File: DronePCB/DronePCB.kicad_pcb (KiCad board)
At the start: 4 copper layers, 161 parts, among them J1 VBUS, J2 PD_SCL, J3 PD_SDA, J4 SysPower, J5 UART, J6 5V, J7 3V3, J8 Battery, J9 USB_C_Receptacle_PowerOnly_6P, M1 Motor_DC, M2 Motor_DC, Q1 AO3400A, Q10 AO3401A, Q11 AO3401A, Q2 AO3400A, Q3 SiS454DN, Q4 SiS454DN, Q5 AO3400A, Q6 AO3400A, Q7 AO3400A, Q8 AO3401A, Q9 AO3401A, U1 RASPBERRY_PI_ZERO_2_W, U10 DRV8231DDAR, U2 CC1101RGPR, U3 BQ24725A, U4 CYPD3177-24LQXQT, U5 DMP3098LSD-13, U6 DMP3098LSD-13, U7 LMR33630BDDA, U8 TSOP45xx, U9 DRV8231DDAR, Y1 Crystal_GND24

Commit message: finished H bridge pcb design
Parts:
- removed R48: 100, Resistor_SMD:R_0603_1608Metric
- removed R49: 10k, Resistor_SMD:R_0603_1608Metric
- moved C46 80.6 mm to (181.5, 150.8)
- moved C48 69.5 mm to (181.5, 143.0)
- moved M1 51.2 mm to (189.1, 134.8), turned to 90 degrees
- moved U9 46.1 mm to (178.8, 134.5)
- moved Q8 44.0 mm to (172.5, 136.7), turned to 90 degrees
- moved C50 39.2 mm to (183.5, 137.5), turned to -90 degrees
- moved C52 38.7 mm to (185.2, 137.5), turned to -90 degrees
- moved Q9 37.6 mm to (172.5, 132.2), turned to -90 degrees
- moved R39 24.2 mm to (176.9, 130.5)
- moved R44 20.5 mm to (172.5, 139.8), turned to 180 degrees
- moved R36 19.5 mm to (166.0, 133.2)
- moved R41 18.5 mm to (172.5, 129.0), turned to 180 degrees
- moved R35 18.3 mm to (166.0, 135.8)
- moved R42 17.1 mm to (166.0, 137.8)
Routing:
- net Net-(Q8-G): track 0.00 -> 16.7 mm, vias 0 -> 2
- net +3V3: track 31.5 -> 47.2 mm, vias 4 -> 6
- net Net-(Q8-D): track 0.00 -> 9.65 mm
- net Net-(Q9-D): track 0.00 -> 9.64 mm
- net Net-(Q10-G): track 6.34 -> 13.5 mm, vias 0 -> 2
- net Net-(U9-IPROPI): track 0.00 -> 2.14 mm
- net GND: vias 37 -> 56
- added copper zone on F.Cu, net Net-(M1-+)
- added copper zone on F.Cu, net Net-(M1--)

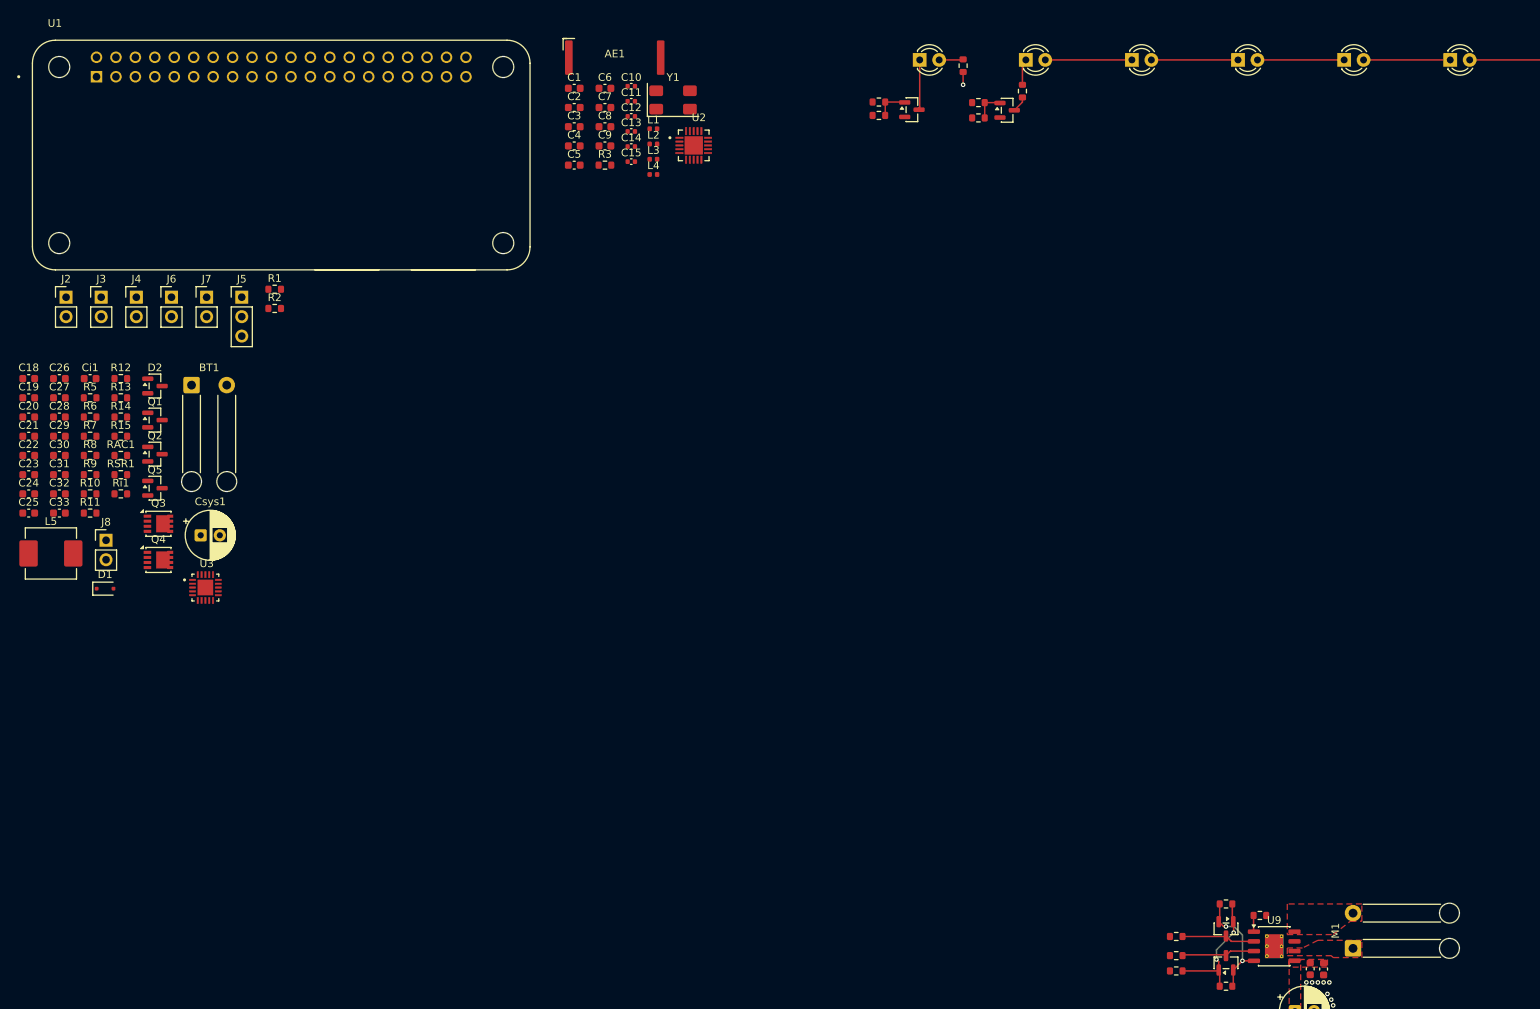
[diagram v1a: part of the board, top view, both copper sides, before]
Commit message: Finished CC1101 Radio Circuit
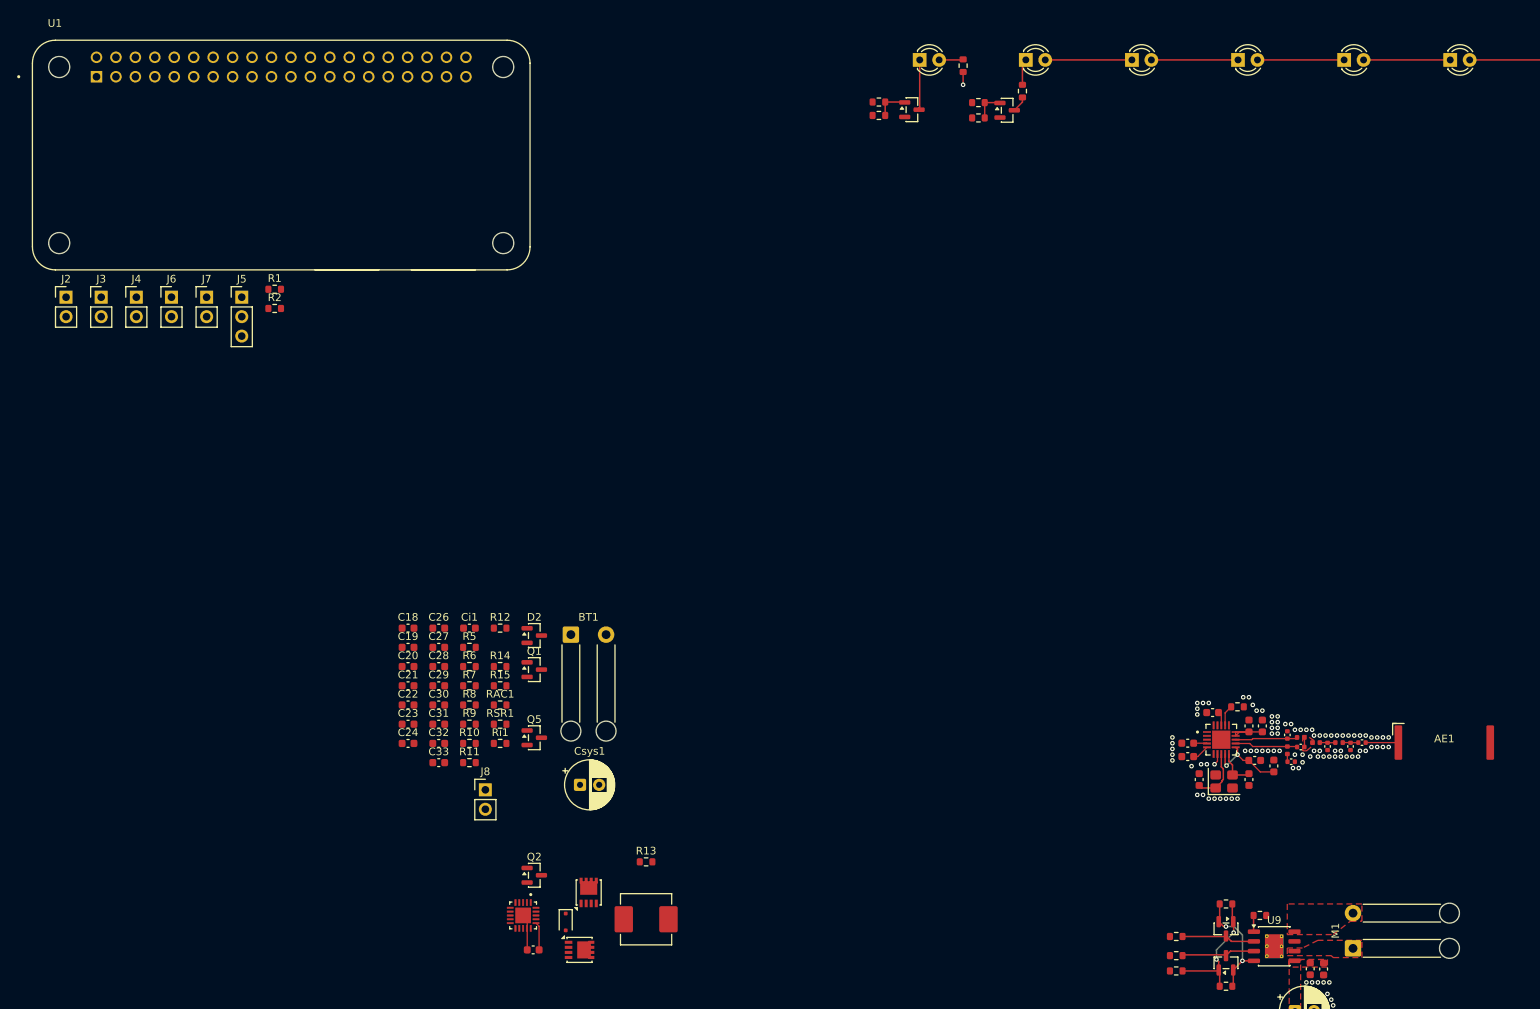
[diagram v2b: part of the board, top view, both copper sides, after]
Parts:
- Y1: value Crystal_GND24 -> NX3225GA; footprint Crystal:Crystal_SMD_0603-4Pin_6.0x3.5mm -> Crystal:Crystal_SMD_3225-4Pin_3.2x2.5mm
- moved AE1 140.5 mm to (201.0, 107.9)
- moved C2 125.5 mm to (178.8, 111.0), turned to 90 degrees
- moved C1 124.9 mm to (176.2, 110.2)
- moved C10 123.4 mm to (181.0, 110.4)
- moved C14 122.3 mm to (188.8, 108.4), turned to -90 degrees
- moved C15 121.9 mm to (190.3, 107.9)
- moved C13 121.3 mm to (185.8, 108.4), turned to -90 degrees
- moved C12 120.1 mm to (182.3, 108.5), turned to 180 degrees
- moved C11 119.1 mm to (180.5, 106.9), turned to -90 degrees
- moved C9 118.0 mm to (175.5, 112.8), turned to -90 degrees
- moved C3 117.9 mm to (175.5, 105.8), turned to 90 degrees
- moved C4 117.6 mm to (177.2, 105.8), turned to 90 degrees
- moved L4 116.3 mm to (187.3, 107.9), turned to 180 degrees
- moved L1 116.0 mm to (180.5, 108.9), turned to -90 degrees
- moved C6 115.8 mm to (167.5, 109.8), turned to 180 degrees
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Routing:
- net +3V3: track 47.2 -> 67.5 mm, vias 6 -> 8
- net Net-(U2-RF_N): track 0.00 -> 8.37 mm
- net Net-(U2-RF_P): track 0.00 -> 8.20 mm
- net XTAL_Q1: track 0.00 -> 7.25 mm
- net XTAL_Q2: track 0.00 -> 5.16 mm
- net GND: track 6.12 -> 10.9 mm, vias 56 -> 141
- net Net-(AE1-A): track 0.00 -> 4.27 mm
- net Net-(D1-A): track 0.00 -> 3.67 mm
- net Net-(U2-RBIAS): track 0.00 -> 2.75 mm
- net Net-(C14-Pad1): track 0.00 -> 2.05 mm
- net Net-(C13-Pad1): track 0.00 -> 2.05 mm
- net Net-(U2-DGUARD): track 0.00 -> 1.82 mm
- net /CC1101Radio/CSN: track 0.00 -> 1.50 mm, vias 0 -> 1
- net Net-(C10-Pad1): track 0.00 -> 1.02 mm
- net Net-(C12-Pad1): track 0.00 -> 1.00 mm
- added copper zone on F.Cu, net Net-(C12-Pad1)

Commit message: All circuits complete
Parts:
- removed BT1: Battery, Connector_Wire:SolderWire-0.5sqmm_1x02_P4.6mm_D0.9mm_OD2.1mm_Relief
- removed Ci1: 2.2 uF, Capacitor_SMD:C_0603_1608Metric
- removed Csys1: 220 uF, Capacitor_THT:CP_Radial_D6.3mm_P2.50mm
- removed the J8 at (75.8, 114.1)
- removed the Q4 at (88.1, 135.0)
- removed the Q5 at (82.1, 107.3)
- removed R10: 316 k ohms, Resistor_SMD:R_0603_1608Metric
- removed R8: 4.02 k ohms, Resistor_SMD:R_0603_1608Metric
- removed Ri1: 2 ohms, Resistor_SMD:R_0603_1608Metric
- added J9: Batt, Connector_Wire:SolderWire-0.25sqmm_1x02_P4.2mm_D0.65mm_OD1.7mm_Relief, F.Cu at (144.6, 121.1)
- added MOSFET1: SIS412DN-T1-GE3, Package_SO:Vishay_PowerPAK_1212-8_Single, F.Cu at (120.0, 109.1)
- added MOSFET2: SIS412DN-T1-GE3, Package_SO:Vishay_PowerPAK_1212-8_Single, F.Cu at (120.0, 104.3)
- added R16: 10 ohms, Resistor_SMD:R_0603_1608Metric, F.Cu at (127.5, 116.3)
- added R17: 7.5 ohms, Resistor_SMD:R_0603_1608Metric, F.Cu at (131.3, 119.8)
- C18: footprint Capacitor_SMD:C_0603_1608Metric -> Capacitor_SMD:C_1210_3225Metric
- C29, C30, C32, C33, C41: footprint Capacitor_SMD:C_0603_1608Metric -> Capacitor_SMD:C_1206_3216Metric
- Q1, Q2: footprint Package_TO_SOT_SMD:SOT-23 -> Package_SO:SO-8_3.9x4.9mm_P1.27mm
- Q3: value SiS454DN -> AO3400A; footprint Package_SO:Vishay_PowerPAK_1212-8_Single -> Package_SO:SO-8_3.9x4.9mm_P1.27mm
- R11: value 10 k ohms -> 100 k ohms
- R12: value 10 ohms -> 316 k ohms
- R13: value 4.02 k ohms -> 10 k ohms
- R15: value 7.5 ohms -> 4.02 k ohms
- R9: value 100 k ohms -> 4.02 k ohms
- moved C53 163.4 mm to (123.1, 33.9), turned to 0 degrees
- moved M2 158.7 mm to (115.5, 49.6), turned to -90 degrees
- moved C51 154.6 mm to (123.0, 41.1), turned to 0 degrees
- moved C55 154.6 mm to (119.3, 46.9), turned to 90 degrees
- moved C57 151.6 mm to (121.0, 46.9), turned to 90 degrees
- moved U10 140.5 mm to (125.8, 49.8), turned to 180 degrees
- moved R39 135.6 mm to (132.3, 44.6), turned to 180 degrees
- moved R47 133.5 mm to (127.5, 53.6), turned to 180 degrees
- moved Q8 132.0 mm to (132.3, 47.6), turned to -90 degrees
- moved R36 128.9 mm to (135.8, 45.6), turned to 180 degrees
- moved Q9 127.3 mm to (132.3, 51.8), turned to 90 degrees
- moved R44 125.2 mm to (135.8, 48.6), turned to 180 degrees
- moved R40 124.3 mm to (132.3, 54.6), turned to 180 degrees
- moved R45 123.1 mm to (135.8, 50.4), turned to 180 degrees
- moved M1 118.2 mm to (265.5, 44.6)
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- renumbered C57 to C43, C43 to C44, C44 to C45, C54 to C46, C55 to C47, C56 to C48, C45 to C49, C46 to C50, C47 to C51, C48 to C52, C49 to C53, C50 to C54, C51 to C55, C52 to C56, C53 to C57, J9 to J8, Q6 to Q4, Q7 to Q5, Q8 to Q6, Q9 to Q7, Q10 to Q8, Q11 to Q9, R16 to R18, R18 to R19, R19 to R20, R20 to R21, R21 to R22, R22 to R23, R23 to R24, R24 to R25, R25 to R26, R26 to R27, R27 to R28, R28 to R29, R29 to R30, R30 to R31, R31 to R32, R32 to R33, R33 to R34, R34 to R35, R45 to R36, R42 to R37, R44 to R38, R50 to R39, R46 to R40, R35 to R42, R36 to R43, R37 to R44, R38 to R45, R39 to R46, R40 to R47
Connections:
- C18 pad 2: Net-(Q1-G) -> Net-(C18-Pad2)
- C19 pad 1: Net-(Q1-S) -> Net-(C19-Pad1)
- C19 pad 2: Net-(Q1-G) -> Net-(C18-Pad2)
- C20 pad 1: Net-(Q2-S) -> Net-(U3-ACP)
- C21 pad 2: Net-(Q2-S) -> Net-(U3-ACP)
- C24 pad 2: Net-(Q4-D) -> Net-(U3-PHASE)
- C27 pad 2: Net-(Q5-S) -> Net-(J9-Pin_1)
- C28 pad 1: Net-(Q5-S) -> Net-(J9-Pin_1)
- C31 pad 1: Net-(Q5-G) (its old number) -> Net-(C31-Pad1)
- C31 pad 2: Net-(Q5-S) -> Net-(J9-Pin_1)
- C32 pad 1: Net-(J8-Pin_2) -> Net-(J9-Pin_1)
- C33 pad 1: Net-(J8-Pin_2) -> Net-(J9-Pin_1)
- L5 pad 1: Net-(Q4-D) -> Net-(U3-PHASE)
- Q1 pad 1: Net-(Q1-G) -> Net-(C19-Pad1)
- Q1 pad 2: Net-(Q1-S) -> Net-(C19-Pad1)
- Q1 pad 3: /Battery Charger/VBUS -> Net-(C19-Pad1)
- Q2 pad 1: Net-(Q1-G) -> Net-(C19-Pad1)
- Q2 pad 2: Net-(Q2-S) -> Net-(C19-Pad1)
- Q2 pad 3: Net-(Q1-S) -> Net-(C19-Pad1)
- Q3 pad 1: Net-(Q4-D) -> Net-(J9-Pin_1)
- Q3 pad 2: Net-(Q4-D) -> Net-(J9-Pin_1)
- Q3 pad 3: Net-(Q4-D) -> Net-(J9-Pin_1)
- Q3 pad 4: Net-(Q3-G) -> Net-(C31-Pad1)
- R11 pad 1: +3V3 -> Net-(U3-ILIM)
- R11 pad 2: ACOK -> GND
- R12 pad 1: Net-(D2-Pad3) -> +3V3
- R12 pad 2: Net-(U3-VCC) -> Net-(U3-ILIM)
- R13 pad 1: Net-(U3-BATDRV) -> +3V3
- R13 pad 2: Net-(Q5-G) (its old number) -> ACOK
- R14 pad 1: Net-(U3-SRP) -> Net-(D2-Pad3)
- R14 pad 2: Net-(C27-Pad1) -> Net-(U3-VCC)
- R15 pad 1: Net-(Q5-S) -> Net-(U3-BATDRV)
- R15 pad 2: Net-(U3-SRN) -> Net-(C31-Pad1)
- R7 pad 1: Net-(Q1-G) -> Net-(C18-Pad2)
- R9 pad 1: Net-(U3-ILIM) -> Net-(C19-Pad1)
- R9 pad 2: GND -> Net-(U3-CMSRC)
- RAC1 pad 1: Net-(Q2-S) -> Net-(U3-ACP)
- RSR1 pad 2: Net-(J8-Pin_2) -> Net-(J9-Pin_1)
- U3 pad 18: Net-(Q3-G) -> Net-(MOSFET2-G)
- U3 pad 19: Net-(Q4-D) -> Net-(U3-PHASE)
- U3 pad 2: Net-(Q2-S) -> Net-(U3-ACP)
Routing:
- net /Battery Charger/VBUS: track 0.00 -> 30.1 mm, vias 0 -> 2
- net Net-(U3-VCC): track 0.00 -> 18.0 mm, vias 0 -> 2
- net Net-(C31-Pad1): track 0.00 -> 17.9 mm, vias 0 -> 2
- net Net-(D1-K): track 0.00 -> 15.2 mm
- net Net-(C18-Pad2): track 0.00 -> 9.52 mm, vias 0 -> 2
- net VDD: track 10.5 -> 1.68 mm
- net Net-(U3-SRN): track 0.00 -> 8.69 mm
- net ACOK: track 0.00 -> 8.13 mm, vias 0 -> 2
- net Net-(U3-CMSRC): track 0.00 -> 7.99 mm, vias 0 -> 2
- net Net-(U3-PHASE): track 0.00 -> 7.64 mm
- net GND: track 10.9 -> 18.1 mm, vias 141 -> 158
- net Net-(MOSFET1-G): track 0.00 -> 6.58 mm, vias 0 -> 2
- net Net-(U3-ACDET): track 0.00 -> 6.22 mm
- net Net-(U3-ACDRV): track 0.00 -> 5.27 mm
- net /Battery Charger/SystemPower: track 0.00 -> 4.47 mm, vias 0 -> 36
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- added copper zone on F.Cu, net /Battery Charger/SystemPower
- added copper zone on In2.Cu, net /Battery Charger/SystemPower
- added copper zone on F.Cu, net /Battery Charger/VBUS
- added copper zone on F.Cu, net Net-(C18-Pad2)
- added copper zone on F.Cu, net Net-(C19-Pad1)
- added copper zone on F.Cu, net Net-(C27-Pad1)
- added copper zone on F.Cu, net Net-(J9-Pin_1)
- added copper zone on F.Cu, net Net-(U3-ACP)
- added copper zone on F.Cu, net Net-(U3-PHASE)
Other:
- board text added: "VIN"

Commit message: Rough board placement complete
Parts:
- D10, D3, D4, D5, D6, D7, D8, D9: footprint LED_THT:LED_D3.0mm_IRBlack -> LED_THT:LED_D5.0mm_IRGrey; moved to B.Cu
- J5, U8: moved to B.Cu
- moved J2 185.3 mm to (200.6, 95.5), turned to 180 degrees
- moved J3 183.9 mm to (204.3, 93.0)
- moved J4 117.0 mm to (135.4, 101.0), turned to 90 degrees
- moved J5 113.4 mm to (156.5, 64.1), turned to -90 degrees
- moved J6 112.6 mm to (144.4, 75.3), turned to 90 degrees
- moved U1 108.1 mm to (173.0, 81.2)
- moved J7 98.8 mm to (135.5, 72.2), turned to 90 degrees
- moved R1 90.6 mm to (136.4, 69.5)
- moved R2 89.7 mm to (136.4, 67.9)
- moved C41 80.8 mm to (147.7, 82.0)
- moved C43 80.8 mm to (162.9, 82.4)
- moved C44 80.8 mm to (162.2, 80.1)
- moved C45 80.8 mm to (148.5, 78.8)
- moved C47 80.8 mm to (151.9, 78.8)
- moved C48 80.8 mm to (150.2, 78.8)
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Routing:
- net Net-(J7-Pin_2): track 0.00 -> 34.3 mm
- net +3V3: track 70.4 -> 91.1 mm
- net +5V: track 0.00 -> 19.0 mm
- net /Battery Charger/SCL: track 1.88 -> 20.1 mm
- net /Battery Charger/SDA: track 2.09 -> 19.8 mm, vias 1 -> 2
- net /USB_PD/SCL: track 1.01 -> 13.2 mm, vias 1 -> 2
- net /USB_PD/SDA: track 1.65 -> 9.57 mm, vias 1 -> 2
- net TX: track 0.00 -> 4.39 mm
- net RX: track 0.00 -> 4.39 mm
- net Net-(D4-K): track 3.43 -> 4.23 mm
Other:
- board outline added: 158 x 68 mm

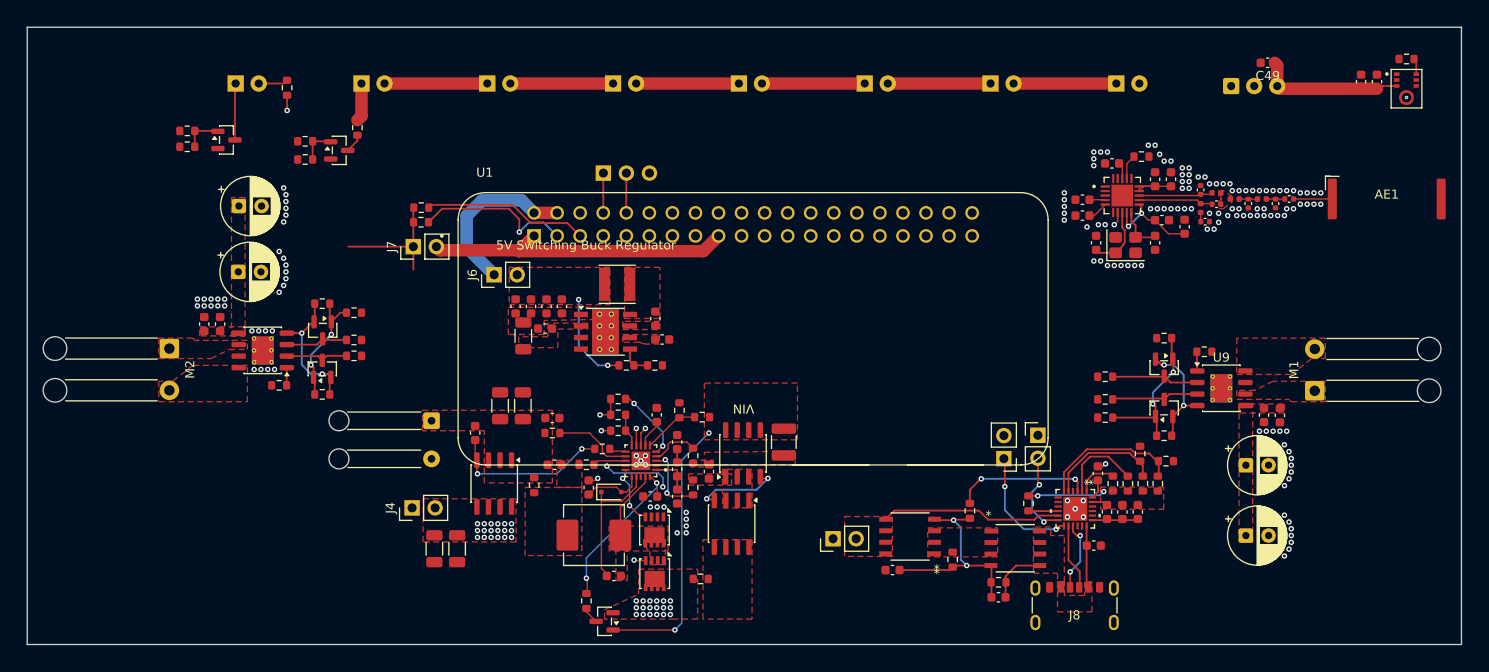
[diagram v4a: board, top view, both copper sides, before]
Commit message: Changed Resistor on IR Blaster | Finished Running DRC on PCB
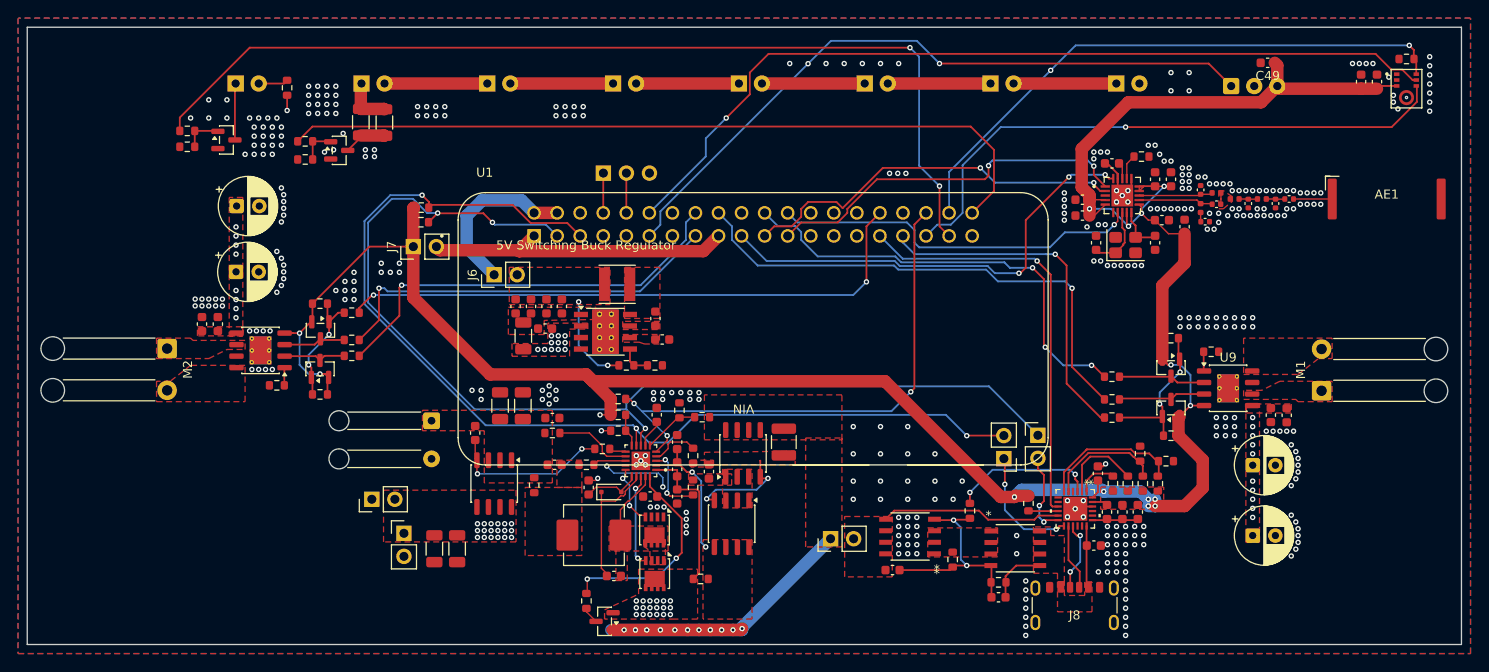
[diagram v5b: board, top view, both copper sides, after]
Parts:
- added J10: SysPower, Connector_PinHeader_2.54mm:PinHeader_1x02_P2.54mm_Vertical, F.Cu at (134.5, 103.8)
- added R48: 68, Resistor_SMD:R_1206_3216Metric, F.Cu at (132.3, 58.5)
- R33: value 35 -> 68; footprint Resistor_SMD:R_0603_1608Metric -> Resistor_SMD:R_1206_3216Metric
- moved J4 4.54 mm to (131.0, 100.0)
- moved C50 0.75 mm to (228.0, 104.0)
- moved C52 0.75 mm to (228.0, 96.2)
- moved C54 0.75 mm to (230.0, 90.7)
- moved C56 0.75 mm to (231.8, 90.8)
- moved M1 0.75 mm to (235.6, 88.0)
- moved Q6 0.75 mm to (219.0, 89.9)
- moved Q7 0.75 mm to (219.0, 85.5)
- moved R37 0.75 mm to (212.5, 91.0)
- moved R38 0.75 mm to (219.0, 93.0)
- moved R41 0.75 mm to (219.0, 82.2)
- moved R42 0.75 mm to (212.5, 89.0)
- moved R43 0.75 mm to (212.5, 86.5)
- moved R46 0.75 mm to (223.4, 83.8)
- moved U9 0.75 mm to (225.3, 87.8)
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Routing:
- net +3V3: track 91.1 -> 260.0 mm, vias 9 -> 15
- net IR_Out: track 0.00 -> 107.6 mm, vias 0 -> 2
- net /Battery Charger/SDA: track 19.8 -> 121.2 mm, vias 2 -> 3
- net /Battery Charger/SCL: track 20.1 -> 117.5 mm, vias 1 -> 3
- net /I2S Microphone/SCK: track 0.00 -> 95.5 mm, vias 0 -> 1
- net IR_Blaster: track 0.00 -> 86.4 mm
- net IR_In: track 0.00 -> 75.9 mm, vias 0 -> 2
- net /H-Bridge/EN_R: track 0.00 -> 65.8 mm, vias 0 -> 2
- net /I2S Microphone/WS: track 0.00 -> 65.0 mm, vias 0 -> 1
- net /I2S Microphone/SD: track 1.77 -> 64.5 mm, vias 0 -> 2
- net IN1_L: track 0.00 -> 57.0 mm, vias 0 -> 1
- net ACOK: track 8.13 -> 59.5 mm, vias 2 -> 3
- net /CC1101Radio/MOSI: track 0.00 -> 50.4 mm, vias 0 -> 3
- net IN2_L: track 0.00 -> 49.7 mm, vias 0 -> 3
- net USB_FAULT: track 0.00 -> 46.8 mm, vias 0 -> 1
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- added copper zone on B.Cu, net GND
- added copper zone on In1.Cu, net GND
- added copper zone on In2.Cu, net VDD
